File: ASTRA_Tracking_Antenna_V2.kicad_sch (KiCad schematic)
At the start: 46 parts, among them J1 Conn_01x02_Socket, J2 24V, J3 24V, J4 24V, J5 5V, J6 Conn_01x04_Socket, M1 Stepper Motor, U2 D24V22F12, U3 DRV8846RGET, U4 AP63203WU-7, U5 AP63205WU-7

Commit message: Tracking Antenna V3 Revisions
Revisions made to TA PCB from recommendations. MCU switched to newer one, SMD parts shifted around, etc.
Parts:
- removed JP1: SolderJumper_3_Open, Jumper:SolderJumper-3_P2.0mm_Open_TrianglePad1.0x1.5mm_NumberLabels, symbol Jumper:SolderJumper_3_Open
- removed U6: ~, Tracking Ant:esp32_devkit_v1, symbol Tracking_Antenna_25_Symbols:ESP32_DOIT_devkit_V1
- added U6: ESP32-S3-DEVKITC-1-N8R8, Tracking Ant:ESP32-S3-DEVKITC-1-N8R8, symbol Tracking_Antenna_25_Symbols:ESP32-S3-DEVKITC-1-N8R8
- C10, C16: footprint Capacitor_SMD:C_0603_1608Metric -> Capacitor_SMD:C_0603_1608Metric_Pad1.08x0.95mm_HandSolder
- C12, C6: value 100nF -> 0.1uF; footprint Capacitor_SMD:C_0603_1608Metric -> Capacitor_SMD:C_0603_1608Metric_Pad1.08x0.95mm_HandSolder
- C15, C9: value 4u7F -> 4.7uF; footprint Capacitor_SMD:C_0603_1608Metric -> Capacitor_SMD:C_0603_1608Metric_Pad1.08x0.95mm_HandSolder
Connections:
- net +24V: now also U5.2 (EN)
- net +5V: now also U6.J1_21 (5V0)
- net ADEC_Driver: now also U6.J1_11 (GPIO18)
- net CurrentScalar0_Driver: now also U6.J1_10 (GPIO17)
- net CurrentScalar1_Driver: now also U6.J1_9 (GPIO16)
- net Decay0_Driver: now also U6.J1_8 (GPIO15)
- net Decay1_Driver: now also U6.J1_6 (GPIO6)
- net Dir_Driver: now also U6.J3_8 (MTDO/GPIO40)
- net Enable_Driver: now also U6.J3_6 (MTMS/GPIO42)
- net GND: now also U6.J1_22 (GND3), U6.J3_1 (GND), U6.J3_21 (GND1), U6.J3_22 (GND2)
- net Micro0_Driver: now also U6.J3_4 (GPIO1)
- net Micro1_Driver: now also U6.J3_5 (GPIO2)
- net NEO_LED_DIN: now also U6.J1_18 (GPIO12)
- net Sensor_SCL: now also U6.J1_15 (GPIO9)
- net Sensor_SDA: now also U6.J1_12 (GPIO8)
- net Sleep_Driver: now also U6.J1_7 (GPIO7)
- net Step_Driver: now also U6.J3_7 (MTDI/GPIO41)
- net nFault_Driver: now also U6.J3_3 (U0RXD/GPIO44)
- no-connect marks 112 -> 128
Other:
- moved on the sheet: C11, C12, C13, C14, C15, C16, J1, J2, J3, J4, J5, L2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

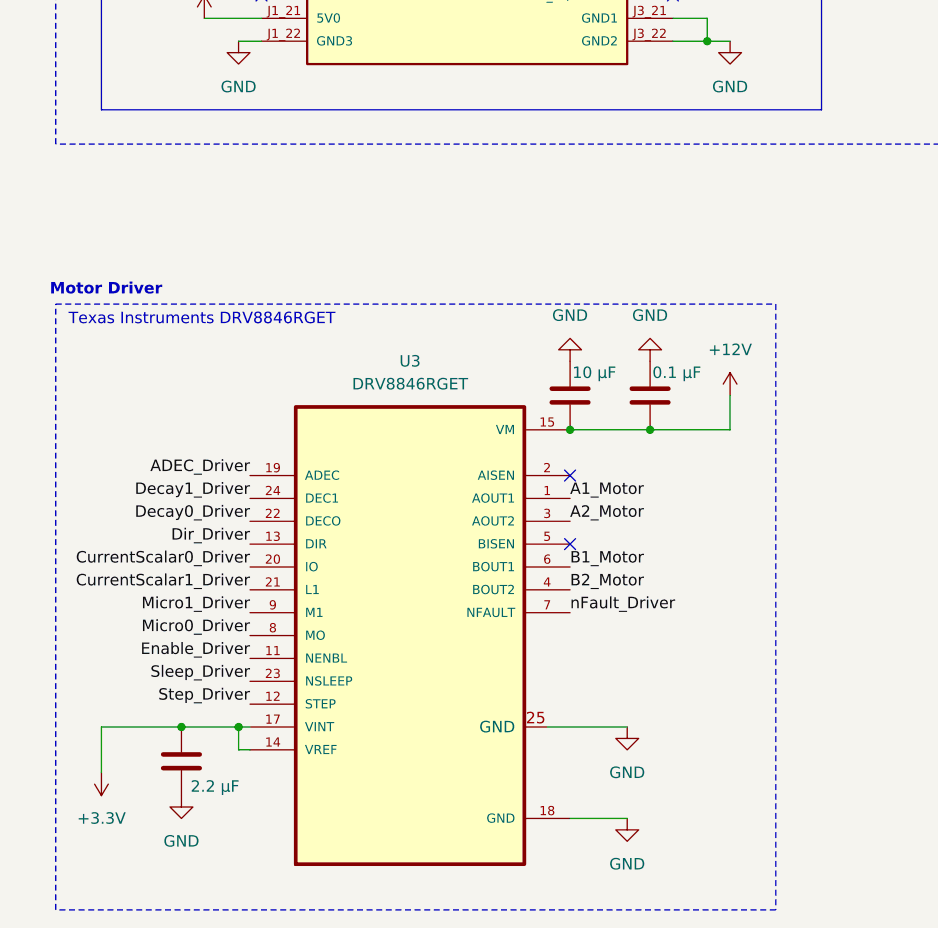
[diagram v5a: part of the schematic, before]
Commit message: V3 Minor Changes
Minor part positioning changes.
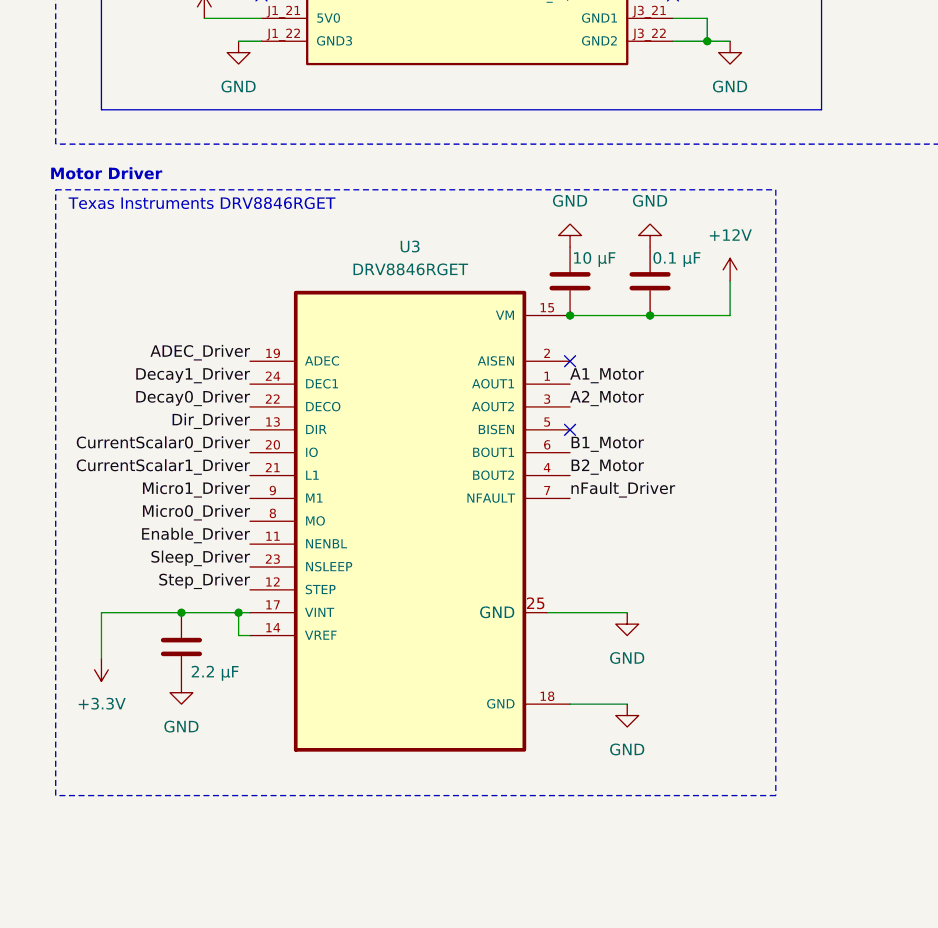
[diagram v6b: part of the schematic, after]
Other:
- moved on the sheet: U3
